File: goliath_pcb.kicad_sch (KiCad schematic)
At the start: 57 parts, among them IC1 MCT9001SD, IC2 MCT9001SD, IC3 MCT9001SD, IC4 MCT9001SD, IC5 MCT9001SD, IC6 MCT9001SD, IC7 MCT9001SD, J1 RJ45_LED, J2 RJ45_LED, J3 RJ45_LED, J4 RJ45_LED, U1 Pico, U2 LM7805_TO220, U3 74HCT244, U4 74HCT244, U5 LTC1298CS8-PBF

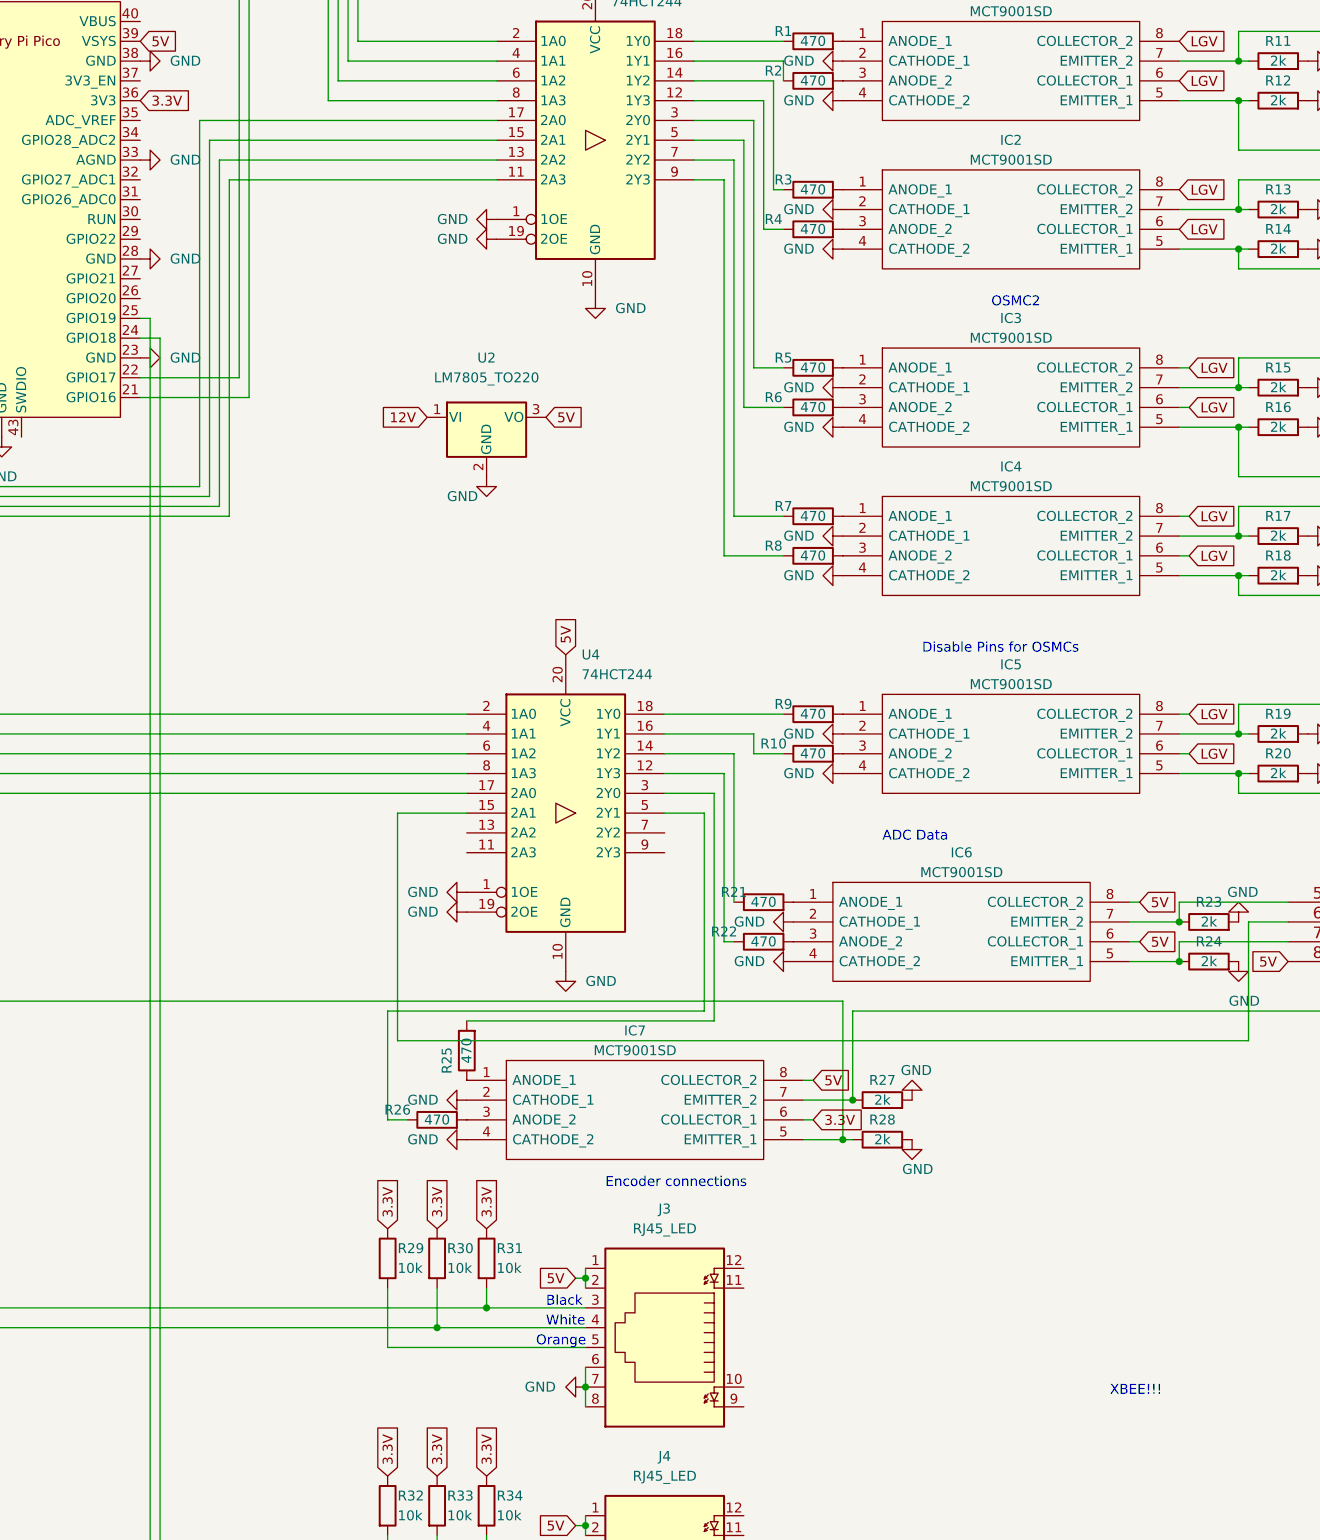
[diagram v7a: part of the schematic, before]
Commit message: Run traces for current version
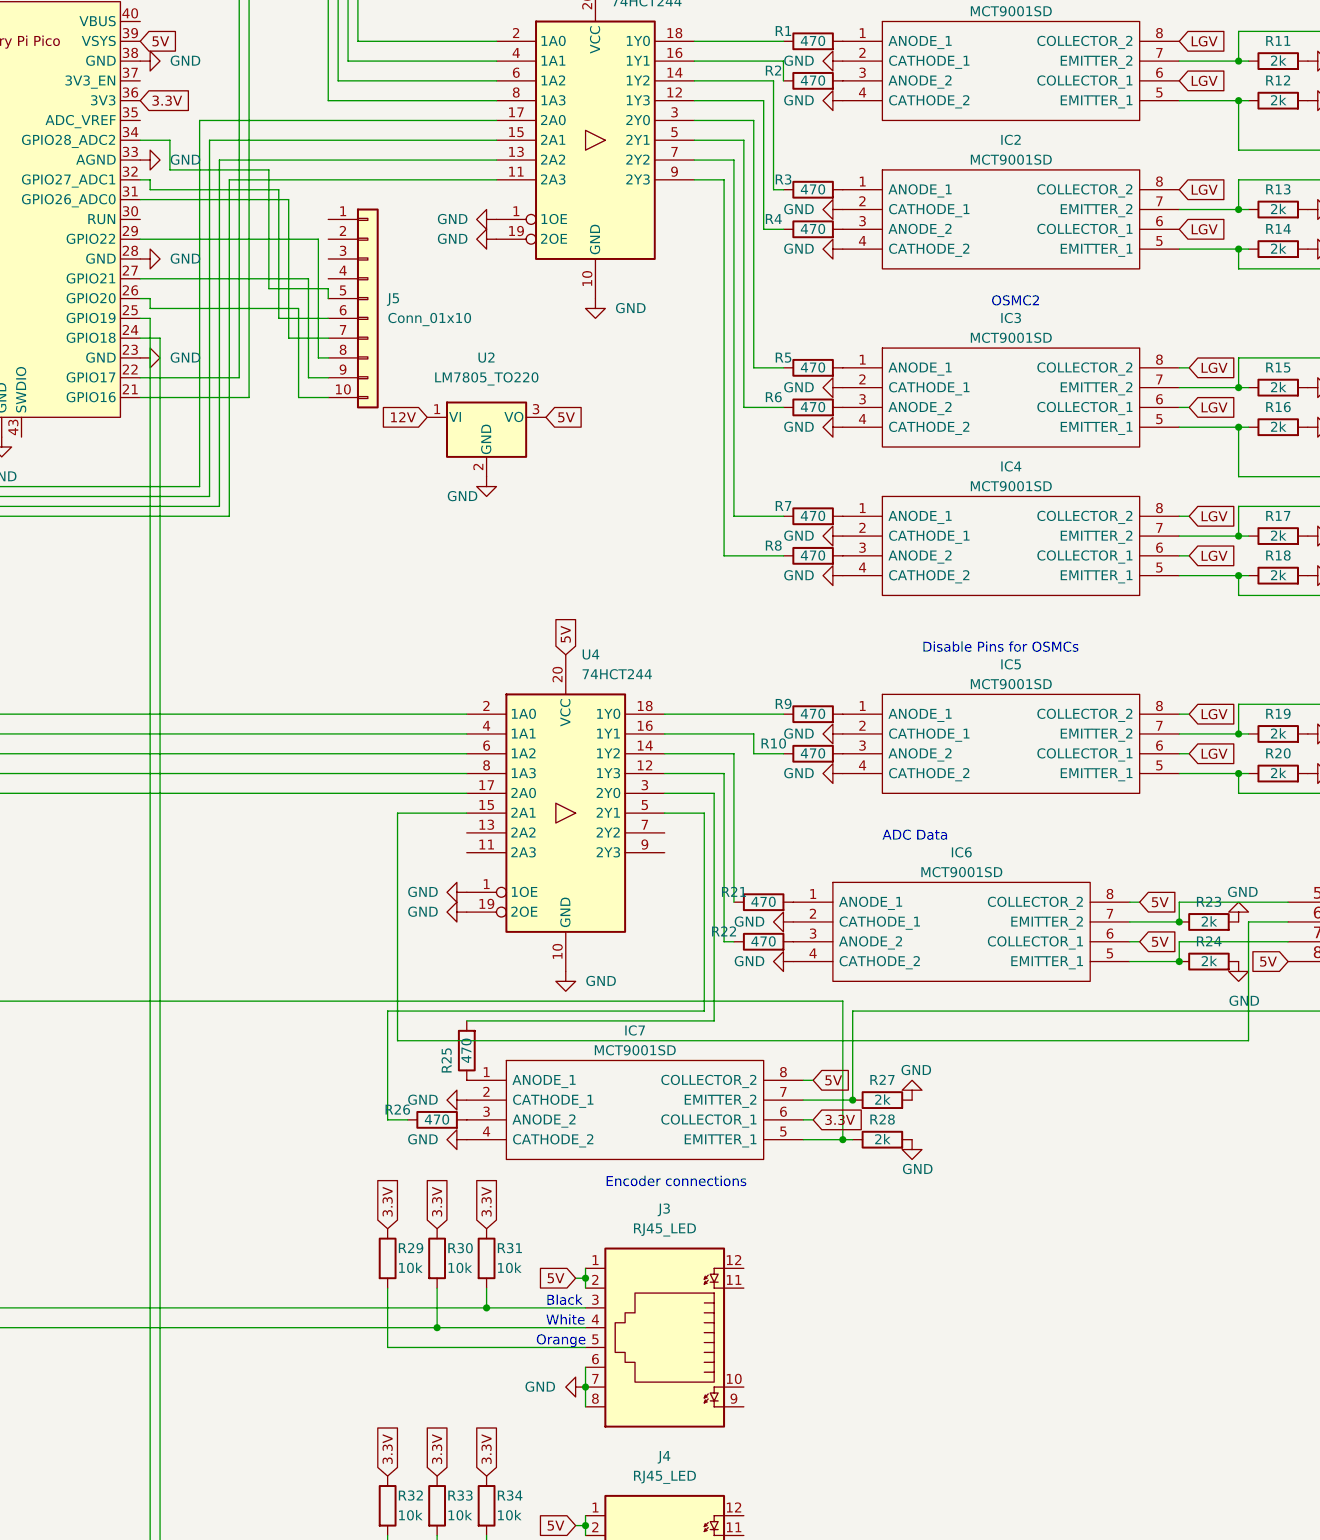
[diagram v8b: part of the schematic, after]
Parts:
- added J5: Conn_01x10, symbol Connector_Generic:Conn_01x10
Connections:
- net at U1.26 (GPIO20): now also J5.10 (Pin_10)
- net at U1.27 (GPIO21): now also J5.9 (Pin_9)
- net at U1.29 (GPIO22): now also J5.8 (Pin_8)
- net at U1.31 (GPIO26_ADC0): now also J5.7 (Pin_7)
- net at U1.32 (GPIO27_ADC1): now also J5.6 (Pin_6)
- net at U1.34 (GPIO28_ADC2): now also J5.5 (Pin_5)
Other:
- note removed: "XBEE!!!"
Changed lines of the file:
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@@
     (stroke (width 0) (type default) (color 0 0 0 0))
   )
+  (wire (pts (xy 91.44 64.77) (xy 72.39 64.77))
+    (stroke (width 0) (type default) (color 0 0 0 0))
+  )
   (wire (pts (xy 139.7 143.51) (xy 144.78 143.51))
     (stroke (width 0) (type default) (color 0 0 0 0))
   )
+  (wire (pts (xy 73.66 78.74) (xy 92.71 78.74))
+    (stroke (width 0) (type default) (color 0 0 0 0))
+  )
   (wire (pts (xy 96.52 34.29) (xy 96.52 52.07))
     (stroke (width 0) (type default) (color 0 0 0 0))
@@
     (stroke (width 0) (type default) (color 0 0 0 0))
   )
+  (wire (pts (xy 92.71 78.74) (xy 92.71 90.17))
+    (stroke (width 0) (type default) (color 0 0 0 0))
+  )
   (wire (pts (xy 129.54 201.93) (xy 129.54 203.2))
     (stroke (width 0) (type default) (color 0 0 0 0))
@@
     (stroke (width 0) (type default) (color 0 0 0 0))
   )
+  (wire (pts (xy 73.66 77.47) (xy 73.66 78.74))
+    (stroke (width 0) (type default) (color 0 0 0 0))
+  )
   (wire (pts (xy 237.49 55.88) (xy 234.95 55.88))
     (stroke (width 0) (type default) (color 0 0 0 0))
@@
     (stroke (width 0) (type default) (color 0 0 0 0))
   )
+  (wire (pts (xy 72.39 74.93) (xy 93.98 74.93))
+    (stroke (width 0) (type default) (color 0 0 0 0))
+  )
   (wire (pts (xy 213.36 43.18) (xy 213.36 46.99))
     (stroke (width 0) (type default) (color 0 0 0 0))
@@
     (stroke (width 0) (type default) (color 0 0 0 0))
   )
+  (wire (pts (xy 90.17 80.01) (xy 96.52 80.01))
+    (stroke (width 0) (type default) (color 0 0 0 0))
+  )
   (wire (pts (xy 36.83 54.61) (xy 34.29 54.61))
     (stroke (width 0) (type default) (color 0 0 0 0))
   )
+  (wire (pts (xy 91.44 82.55) (xy 91.44 64.77))
+    (stroke (width 0) (type default) (color 0 0 0 0))
+  )
   (wire (pts (xy 280.67 160.02) (xy 270.51 160.02))
     (stroke (width 0) (type default) (color 0 0 0 0))
@@
     (stroke (width 0) (type default) (color 0 0 0 0))
   )
+  (wire (pts (xy 96.52 82.55) (xy 91.44 82.55))
+    (stroke (width 0) (type default) (color 0 0 0 0))
+  )
   (wire (pts (xy 205.74 71.12) (xy 213.36 71.12))
     (stroke (width 0) (type default) (color 0 0 0 0))
@@
     (stroke (width 0) (type default) (color 0 0 0 0))
   )
+  (wire (pts (xy 72.39 57.15) (xy 76.2 57.15))
+    (stroke (width 0) (type default) (color 0 0 0 0))
+  )
   (wire (pts (xy 232.41 144.78) (xy 232.41 53.34))
     (stroke (width 0) (type default) (color 0 0 0 0))
@@
     (stroke (width 0) (type default) (color 0 0 0 0))
   )
+  (wire (pts (xy 76.2 60.96) (xy 88.9 60.96))
+    (stroke (width 0) (type default) (color 0 0 0 0))
+  )
   (wire (pts (xy 97.79 49.53) (xy 118.11 49.53))
     (stroke (width 0) (type default) (color 0 0 0 0))
@@
     (stroke (width 0) (type default) (color 0 0 0 0))
   )
+  (wire (pts (xy 95.25 69.85) (xy 72.39 69.85))
+    (stroke (width 0) (type default) (color 0 0 0 0))
+  )
   (wire (pts (xy 36.83 49.53) (xy 34.29 49.53))
     (stroke (width 0) (type default) (color 0 0 0 0))
@@
     (stroke (width 0) (type default) (color 0 0 0 0))
   )
+  (wire (pts (xy 73.66 62.23) (xy 73.66 63.5))
+    (stroke (width 0) (type default) (color 0 0 0 0))
+  )
   (wire (pts (xy 213.36 66.04) (xy 213.36 62.23))
     (stroke (width 0) (type default) (color 0 0 0 0))
@@
     (stroke (width 0) (type default) (color 0 0 0 0))
   )
+  (wire (pts (xy 92.71 90.17) (xy 96.52 90.17))
+    (stroke (width 0) (type default) (color 0 0 0 0))
+  )
   (wire (pts (xy 316.23 49.53) (xy 326.39 49.53))
     (stroke (width 0) (type default) (color 0 0 0 0))
@@
     (stroke (width 0) (type default) (color 0 0 0 0))
   )
+  (wire (pts (xy 90.17 63.5) (xy 90.17 80.01))
+    (stroke (width 0) (type default) (color 0 0 0 0))
+  )
   (wire (pts (xy 231.14 95.25) (xy 231.14 142.24))
     (stroke (width 0) (type default) (color 0 0 0 0))
@@
     (stroke (width 0) (type default) (color 0 0 0 0))
   )
+  (wire (pts (xy 95.25 85.09) (xy 95.25 69.85))
+    (stroke (width 0) (type default) (color 0 0 0 0))
+  )
   (wire (pts (xy 72.39 87.63) (xy 85.09 87.63))
     (stroke (width 0) (type default) (color 0 0 0 0))
@@
     (stroke (width 0) (type default) (color 0 0 0 0))
   )
+  (wire (pts (xy 72.39 77.47) (xy 73.66 77.47))
+    (stroke (width 0) (type default) (color 0 0 0 0))
+  )
   (wire (pts (xy 213.36 138.43) (xy 213.36 140.97))
     (stroke (width 0) (type default) (color 0 0 0 0))
@@
     (stroke (width 0) (type default) (color 0 0 0 0))
   )
+  (wire (pts (xy 93.98 74.93) (xy 93.98 87.63))
+    (stroke (width 0) (type default) (color 0 0 0 0))
+  )
   (wire (pts (xy 205.74 52.07) (xy 213.36 52.07))
     (stroke (width 0) (type default) (color 0 0 0 0))
   )
+  (wire (pts (xy 73.66 63.5) (xy 90.17 63.5))
+    (stroke (width 0) (type default) (color 0 0 0 0))
+  )
   (wire (pts (xy 116.84 238.76) (xy 74.93 238.76))
     (stroke (width 0) (type default) (color 0 0 0 0))
@@
     (stroke (width 0) (type default) (color 0 0 0 0))
   )
+  (wire (pts (xy 96.52 76.2) (xy 96.52 77.47))
+    (stroke (width 0) (type default) (color 0 0 0 0))
+  )
   (wire (pts (xy 129.54 214.63) (xy 129.54 217.17))
     (stroke (width 0) (type default) (color 0 0 0 0))
@@
     (stroke (width 0) (type default) (color 0 0 0 0))
   )
+  (wire (pts (xy 76.2 57.15) (xy 76.2 60.96))
+    (stroke (width 0) (type default) (color 0 0 0 0))
+  )
   (wire (pts (xy 97.79 33.02) (xy 97.79 49.53))
     (stroke (width 0) (type default) (color 0 0 0 0))
@@
     (stroke (width 0) (type default) (color 0 0 0 0))
   )
+  (wire (pts (xy 72.39 62.23) (xy 73.66 62.23))
+    (stroke (width 0) (type default) (color 0 0 0 0))
+  )
   (wire (pts (xy 151.13 135.89) (xy 154.94 135.89))
     (stroke (width 0) (type default) (color 0 0 0 0))
@@
     (stroke (width 0) (type default) (color 0 0 0 0))
   )
+  (wire (pts (xy 88.9 76.2) (xy 96.52 76.2))
+    (stroke (width 0) (type default) (color 0 0 0 0))
+  )
   (wire (pts (xy 147.32 110.49) (xy 154.94 110.49))
     (stroke (width 0) (type default) (color 0 0 0 0))
@@
     (stroke (width 0) (type default) (color 0 0 0 0))
   )
+  (wire (pts (xy 96.52 85.09) (xy 95.25 85.09))
+    (stroke (width 0) (type default) (color 0 0 0 0))
+  )
   (wire (pts (xy 233.68 140.97) (xy 233.68 97.79))
     (stroke (width 0) (type default) (color 0 0 0 0))
@@
     (stroke (width 0) (type default) (color 0 0 0 0))
   )
+  (wire (pts (xy 93.98 87.63) (xy 96.52 87.63))
+    (stroke (width 0) (type default) (color 0 0 0 0))
+  )
   (wire (pts (xy 116.84 238.76) (xy 129.54 238.76))
     (stroke (width 0) (type default) (color 0 0 0 0))
@@
     (stroke (width 0) (type default) (color 0 0 0 0))
   )
+  (wire (pts (xy 88.9 60.96) (xy 88.9 76.2))
+    (stroke (width 0) (type default) (color 0 0 0 0))
+  )
   (wire (pts (xy 205.74 46.99) (xy 213.36 46.99))
     (stroke (width 0) (type default) (color 0 0 0 0))
@@
     (effects (font (size 1.27 1.27)) (justify left bottom))
   )
-  (text "XBEE!!!" (at 196.85 218.44 0)
-    (effects (font (size 1.27 1.27)) (justify left bottom))
-  )
   (text "Disable Pins for OSMCs" (at 172.72 123.19 0)
     (effects (font (size 1.27 1.27)) (justify left bottom))
@@
     (pin "2")
   )
+  (symbol (lib_id "Connector_Generic:Conn_01x10") (at 101.6 77.47 0) (unit 1)
+    (in_bom yes) (on_board yes) (fields_autoplaced)
+    (property "Reference" "J5" (id 0) (at 104.14 77.4699 0)
+      (effects (font (size 1.27 1.27)) (justify left))
+    )
+    (property "Value" "Conn_01x10" (id 1) (at 104.14 80.0099 0)
+      (effects (font (size 1.27 1.27)) (justify left))
+    )
+    (property "Footprint" "" (id 2) (at 101.6 77.47 0)
+      (effects (font (size 1.27 1.27)) hide)
+    )
+    (property "Datasheet" "~" (id 3) (at 101.6 77.47 0)
+      (effects (font (size 1.27 1.27)) hide)
+    )
+    (pin "1")
+    (pin "10")
+    (pin "2")
+    (pin "3")
+    (pin "4")
+    (pin "5")
+    (pin "6")
+    (pin "7")
+    (pin "8")
+    (pin "9")
+  )
   (symbol (lib_id "Device:R") (at 114.3 173.99 180) (unit 1)
     (in_bom yes) (on_board yes)
@@
       (reference "J4") (unit 1) (value "RJ45_LED") (footprint "Connector_RJ:RJ45_Amphenol_RJHSE538X")
     )
+    (path "/e94b1b04-bf52-40ee-8669-6cb034950a3a"
+      (reference "J5") (unit 1) (value "Conn_01x10") (footprint "")
+    )
     (path "/6b6ef087-df10-4bb6-b2b6-405ccc1c445d"
